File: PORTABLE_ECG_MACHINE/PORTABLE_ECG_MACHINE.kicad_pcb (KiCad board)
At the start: 2 copper layers, 25.5 x 64.8 mm, 92 parts, among them IC1 AD8232ACPZ, J1 UART, J2 AudioJack3, J3 Li-Ion 3.7 CONN, J4 USB_C_Receptacle_USB2.0, J5 Conn_01x06_Male, Q1 BSS138, Q2 BSS138, SW1 SW_SPDT, U1 SSD1306, U2 CP2102-GM, U3 ATmega328PB-A, U4 TC1262-33, U5 TP4056, Y1 16MHZ

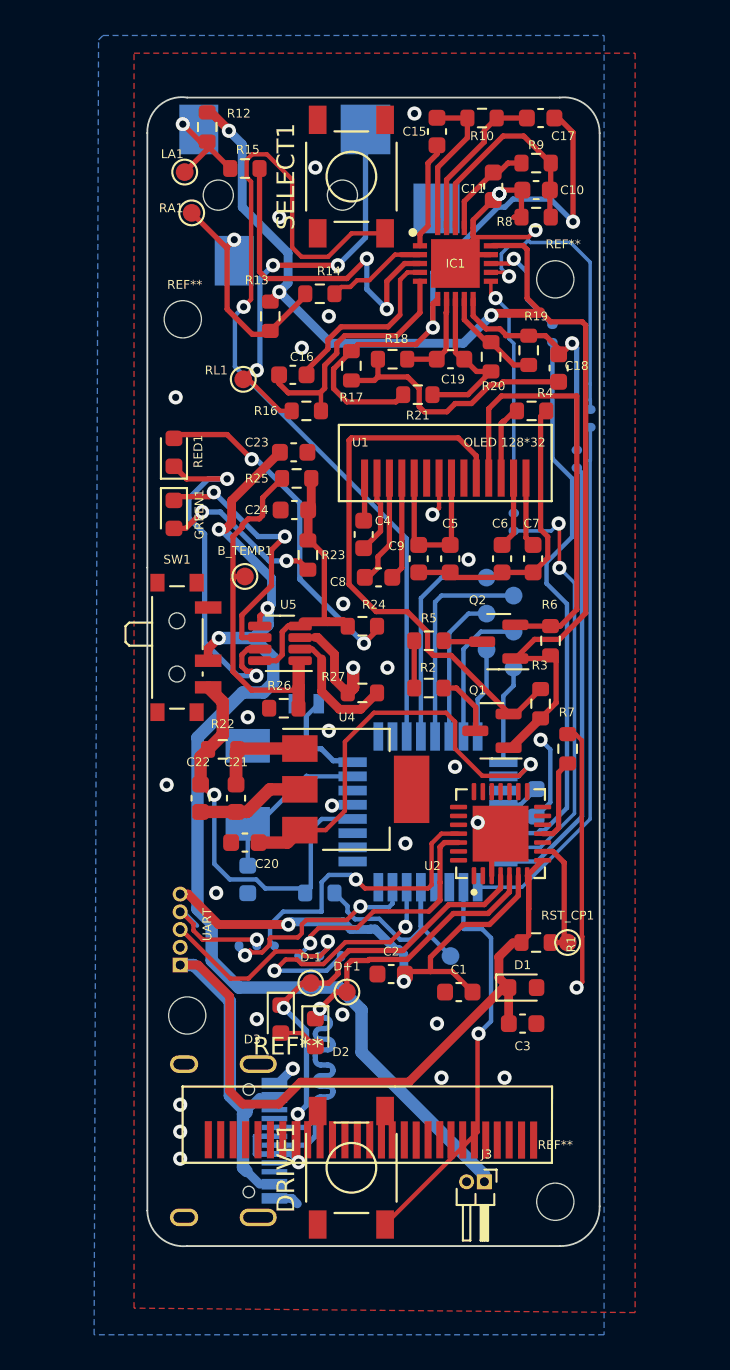
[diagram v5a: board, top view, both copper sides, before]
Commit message: version 2.0 | oled 128*64
new version created substituted 128*64 instead of 128*64. EESCHEMA and PCBNEW completed. OLED 128*64 3D MODEL need to fix
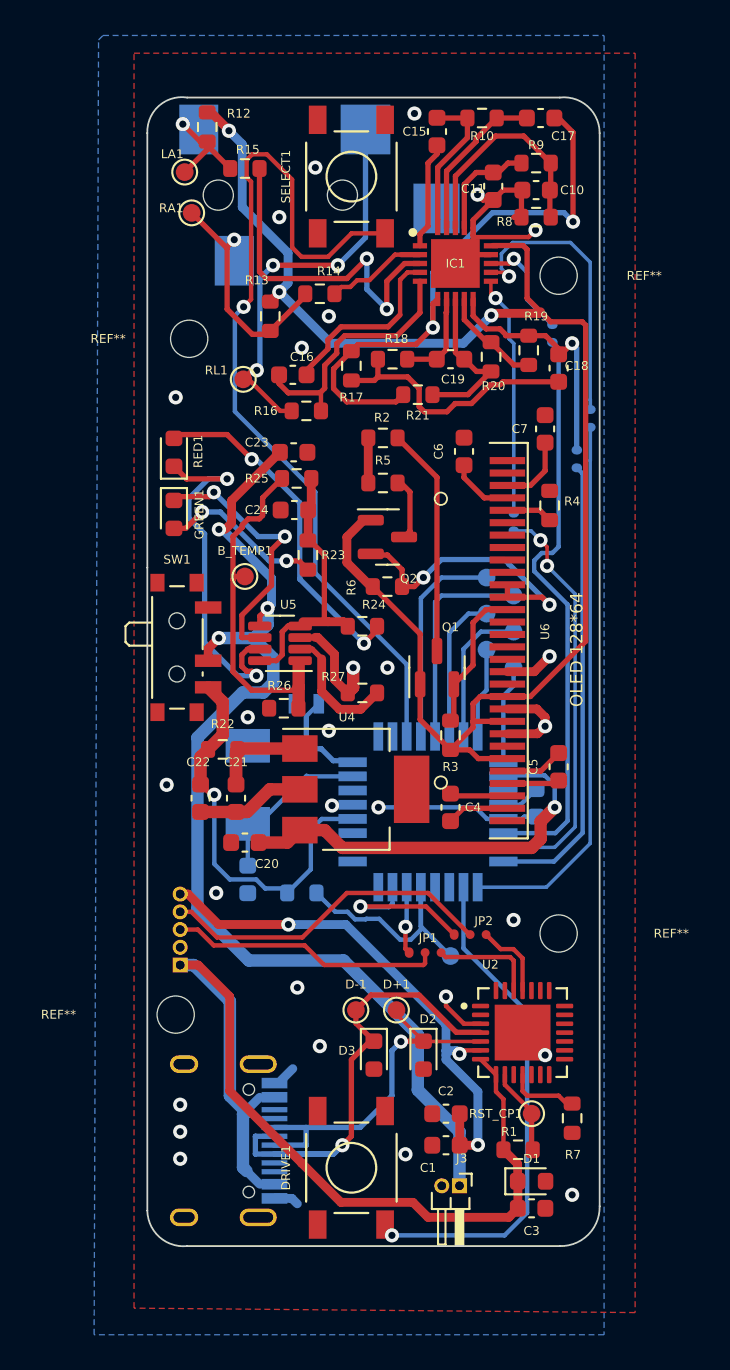
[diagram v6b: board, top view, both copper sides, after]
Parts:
- removed C8, C9: 1uf, Capacitor_SMD:C_0603_1608Metric
- removed the REF** at (107.0, 34.8)
- removed the REF** at (86.0, 37.0)
- removed the REF** at (91.9, 78.5)
- removed the REF** at (107.0, 86.8)
- removed U1: SSD1306, SSD1306:SSD1306
- removed UART: MountingHole_2.1mm, MountingHole:MountingHole_2.1mm
- added REF**: MountingHole_2.1mm, MountingHole:MountingHole_2.1mm, F.Cu at (107.2, 71.6)
- added REF**: MountingHole_2.1mm, MountingHole:MountingHole_2.1mm, F.Cu at (107.2, 34.5)
- added REF**: MountingHole_2.1mm, MountingHole:MountingHole_2.1mm, F.Cu at (85.6, 76.2)
- added REF**: MountingHole_2.1mm, MountingHole:MountingHole_2.1mm, F.Cu at (86.4, 38.1)
- added U6: SSD1306, Display:OLED-128O064D, F.Cu at (104.3, 55.1)
- C6: value 10uf -> 2.2UF
- C7: value 10uf -> 10UF
- JP1, JP2: moved to F.Cu
- R4: value 330k -> 390K
- moved R7 20.8 mm to (108.0, 82.0), turned to -90 degrees
- moved C4 16.1 mm to (101.1, 64.5)
- moved R2 14.3 mm to (97.3, 43.7)
- moved JP2 13.4 mm to (101.6, 69.1)
- moved C5 13.2 mm to (107.2, 62.2)
- moved R1 11.7 mm to (104.9, 83.8)
- moved U2 11.3 mm to (105.2, 77.2), turned to 0 degrees
- moved D1 10.9 mm to (105.7, 85.6)
- moved C3 10.4 mm to (105.7, 87.1)
- moved RST_CP1 9.86 mm to (105.7, 81.8)
- moved R6 9.69 mm to (97.5, 52.1), turned to 0 degrees
- moved R5 9.26 mm to (97.3, 46.2)
- moved C1 8.67 mm to (100.8, 83.6)
- moved Q2 8.61 mm to (97.5, 49.3), turned to 0 degrees
- moved C2 8.46 mm to (100.8, 81.8)
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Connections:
- net SCL_3.3 renamed /SCL_3.3
- net SCL_5 renamed /SCL_5
- net SDA_5 renamed /SDA_5
- net USB_D+ renamed /USB_D+
- net USB_D- renamed /USB_D-
- C5 pad 1: GND -> Net-(C5-Pad1)
- C6 pad 1: GND -> Net-(C6-Pad1)
- C6 pad 2: Net-(C6-Pad2) -> GND
- C7 pad 1: GND -> Net-(C7-Pad1)
- C7 pad 2: Net-(C7-Pad2) -> GND
- Q2 pad 2: SDA_3.3 -> /SDA_3.3
- R6 pad 1: SDA_3.3 -> 3.3V
- R6 pad 2: 3.3V -> /SDA_3.3
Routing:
- net GND: track 77.9 -> 52.1 mm, vias 33 -> 28
- net SDA_3.3: track 25.0 -> 0.00 mm
- net /SCL_3.3: track 32.1 -> 8.29 mm
- net 3.3V: track 68.3 -> 88.8 mm
- net /SDA_3.3: track 0.00 -> 16.3 mm, vias 0 -> 2
- net /USB_D+: track 33.0 -> 20.3 mm
- net /CP_RXD: track 17.0 -> 4.43 mm, vias 1 -> 0
- net Net-(J1-Pad4): track 6.81 -> 19.0 mm, vias 1 -> 0
- net /AT_RXD: track 15.0 -> 3.80 mm, vias 2 -> 1
- net /SCL_5: track 3.60 -> 12.9 mm
- net /CP_TXD: track 13.7 -> 5.97 mm, vias 1 -> 0
- net Net-(C5-Pad2): track 9.58 -> 3.32 mm
- net Net-(C8-Pad1): track 6.09 -> 0.00 mm
- net Net-(DRIVE1-Pad3): track 22.7 -> 28.8 mm
- net Net-(C8-Pad2): track 5.82 -> 0.00 mm
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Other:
- board text added: "OLED 128*64"
- board text removed: "OLED 128*32"

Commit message: BOM-README update
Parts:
- C14: footprint Crystal:Crystal_SMD_2012-2Pin_2.0x1.2mm -> Capacitor_SMD:C_0603_1608Metric
- C2: value 100nf -> .1uf
- C6: value 2.2UF -> 2.2uf
- C7: value 10UF -> 10uf
- J2: value AudioJack3 -> ECG PROBE
- R11, R7: value 10K -> 10k
- R19: value 1M -> 1m
- R20: value 330K -> 330k
- R21: value 100K -> 100k
- R4: value 390K -> 390k
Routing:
- net Net-(J1-Pad4): track 19.0 -> 20.3 mm
- net /AT_TXD: track 8.78 -> 7.60 mm
- net GND: vias 28 -> 27
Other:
- board text added: "JLCJLCJLCJLC"

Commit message: REV 3
footprint change tp4056,add new 3d model oled 128*64,kicad render imgs add
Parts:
- R19: value 1m -> 1M
- U4: value TC1262-33 -> LM3940IMP-3.3/NOPB
- U5: footprint Package_TO_SOT_SMD:TSOT-23-8 -> tp4056 ftprnt:SOP127P600X175-9N
- moved R24 7.07 mm to (94.2, 47.5), turned to 90 degrees
- moved C20 2.12 mm to (89.9, 68.6)
- moved C22 2.04 mm to (86.9, 66.0)
- moved C21 2.04 mm to (88.9, 66.0)
- moved U5 2.00 mm to (93.5, 55.4)
- moved B_TEMP1 1.80 mm to (90.1, 49.8)
- moved U4 1.79 mm to (95.5, 65.3)
- moved R22 1.67 mm to (87.1, 62.5)
- moved R6 1.48 mm to (98.8, 51.3)
- moved R27 1.43 mm to (96.5, 59.4)
- moved Q2 1.14 mm to (98.6, 48.8)
- moved Y1 1.14 mm to (90.7, 63.8)
- moved C23 0.90 mm to (91.7, 45.2)
- moved R25 0.89 mm to (91.9, 46.7)
- moved R26 0.72 mm to (92.2, 59.4)
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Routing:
- net GND: track 52.1 -> 43.1 mm, vias 27 -> 26
- net /BATTERY +VE: track 63.3 -> 56.7 mm
- net Net-(R24-Pad1): track 19.5 -> 13.0 mm, vias 2 -> 0
- net Net-(RED1-Pad1): track 20.9 -> 15.6 mm, vias 2 -> 0
- net Net-(C24-Pad1): track 15.2 -> 20.3 mm, vias 0 -> 2
- net Net-(B_TEMP1-Pad1): track 19.9 -> 23.3 mm, vias 0 -> 2
- net VCC: track 22.8 -> 25.5 mm
- net Net-(GREEN1-Pad2): track 9.28 -> 6.83 mm
- net Net-(GREEN1-Pad1): track 15.2 -> 13.4 mm, vias 2 -> 1
- net 3.3V: track 88.8 -> 90.1 mm
- net Net-(R27-Pad2): track 7.21 -> 6.19 mm
- net /SDA_3.3: track 16.3 -> 15.3 mm
- net Net-(C14-Pad1): track 10.1 -> 9.19 mm
- net /SDA_5: track 3.59 -> 2.90 mm
- net +3V3: track 23.3 -> 24.0 mm
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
